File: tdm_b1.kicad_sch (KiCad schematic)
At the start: 8 parts, among them J1 Conn_02x17_Odd_Even, J8 Conn_02x08_Odd_Even, J9 Conn_02x15_Odd_Even

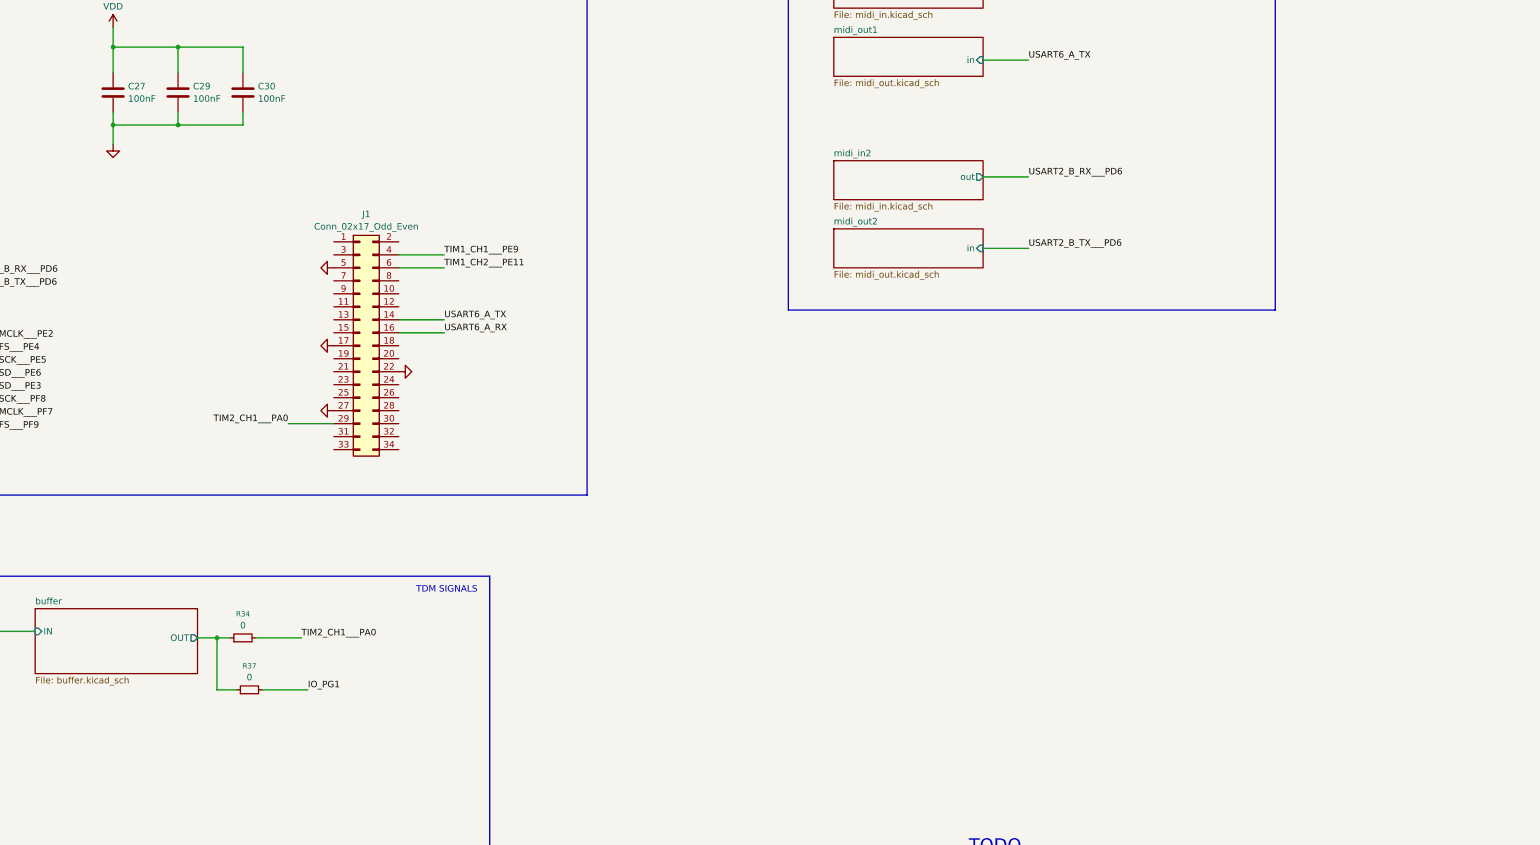
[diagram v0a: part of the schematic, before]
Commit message: adding subproject, breakout board for nucleo
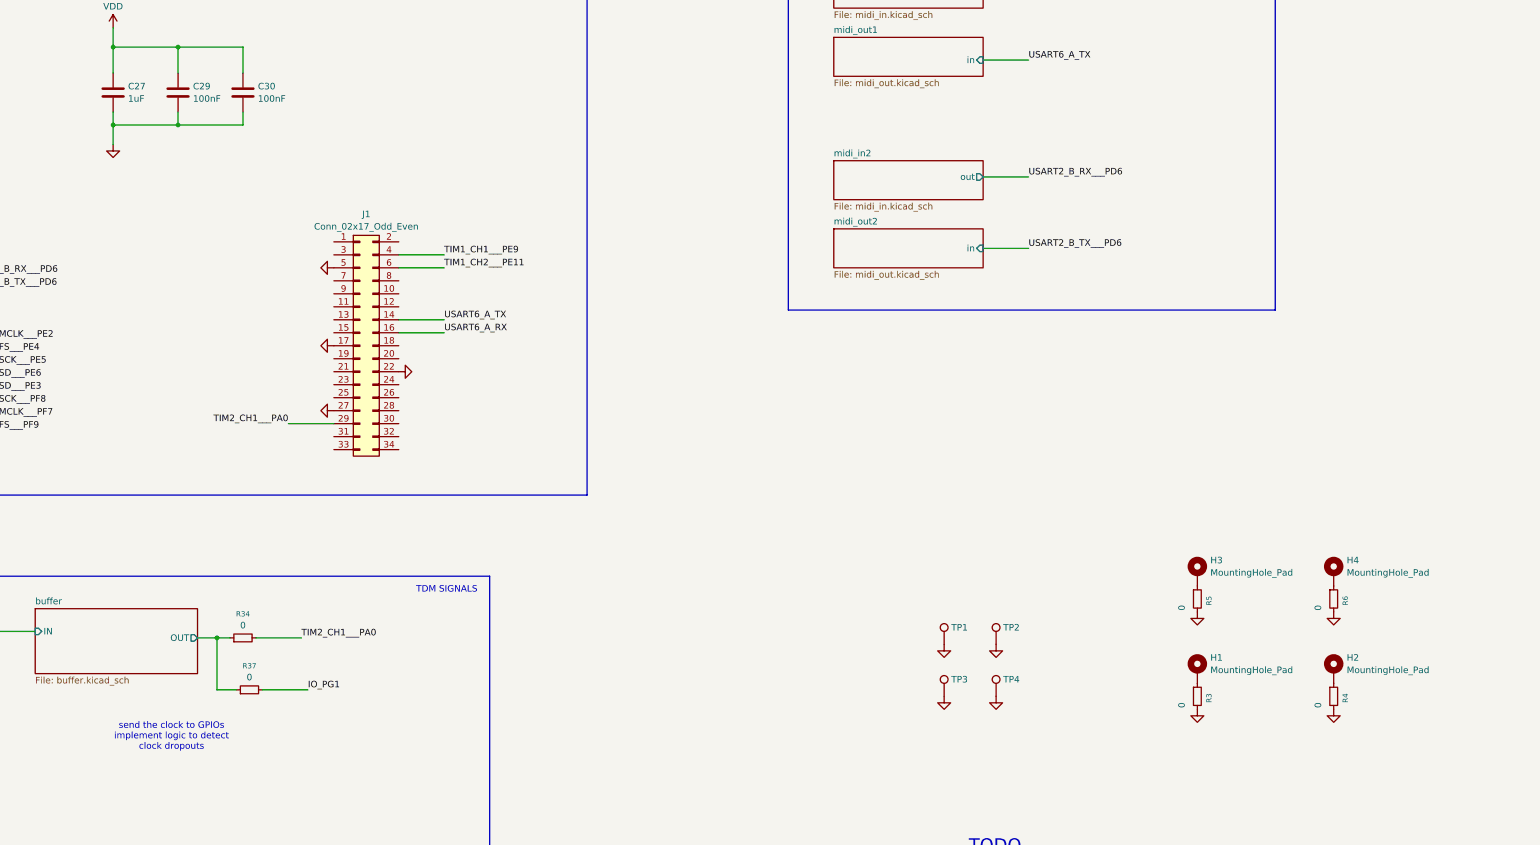
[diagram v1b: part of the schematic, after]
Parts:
- added H1, H2, H3, H4: MountingHole_Pad, MountingHole:MountingHole_3.2mm_M3_DIN965_Pad, symbol Mechanical:MountingHole_Pad
- added R3, R4, R5, R6: 0, Resistor_SMD:R_0603_1608Metric, symbol Device:R_Small
- added TP1, TP2, TP3, TP4: TestPoint, TestPoint:TestPoint_THTPad_D1.5mm_Drill0.7mm, symbol Connector:TestPoint
- C27: value 100nF -> 1uF
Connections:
- net GND: now also R3.2, R4.2, R5.2, R6.2, TP1.1, TP2.1, TP3.1, TP4.1
- new net: H2.1, R4.1
- new net: H1.1, R3.1
- new net: H4.1, R6.1
- new net: H3.1, R5.1
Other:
- note added: "send the clock to GPIOs implement logic to detect clock dropouts"
